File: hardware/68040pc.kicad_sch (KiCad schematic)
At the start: 1 part

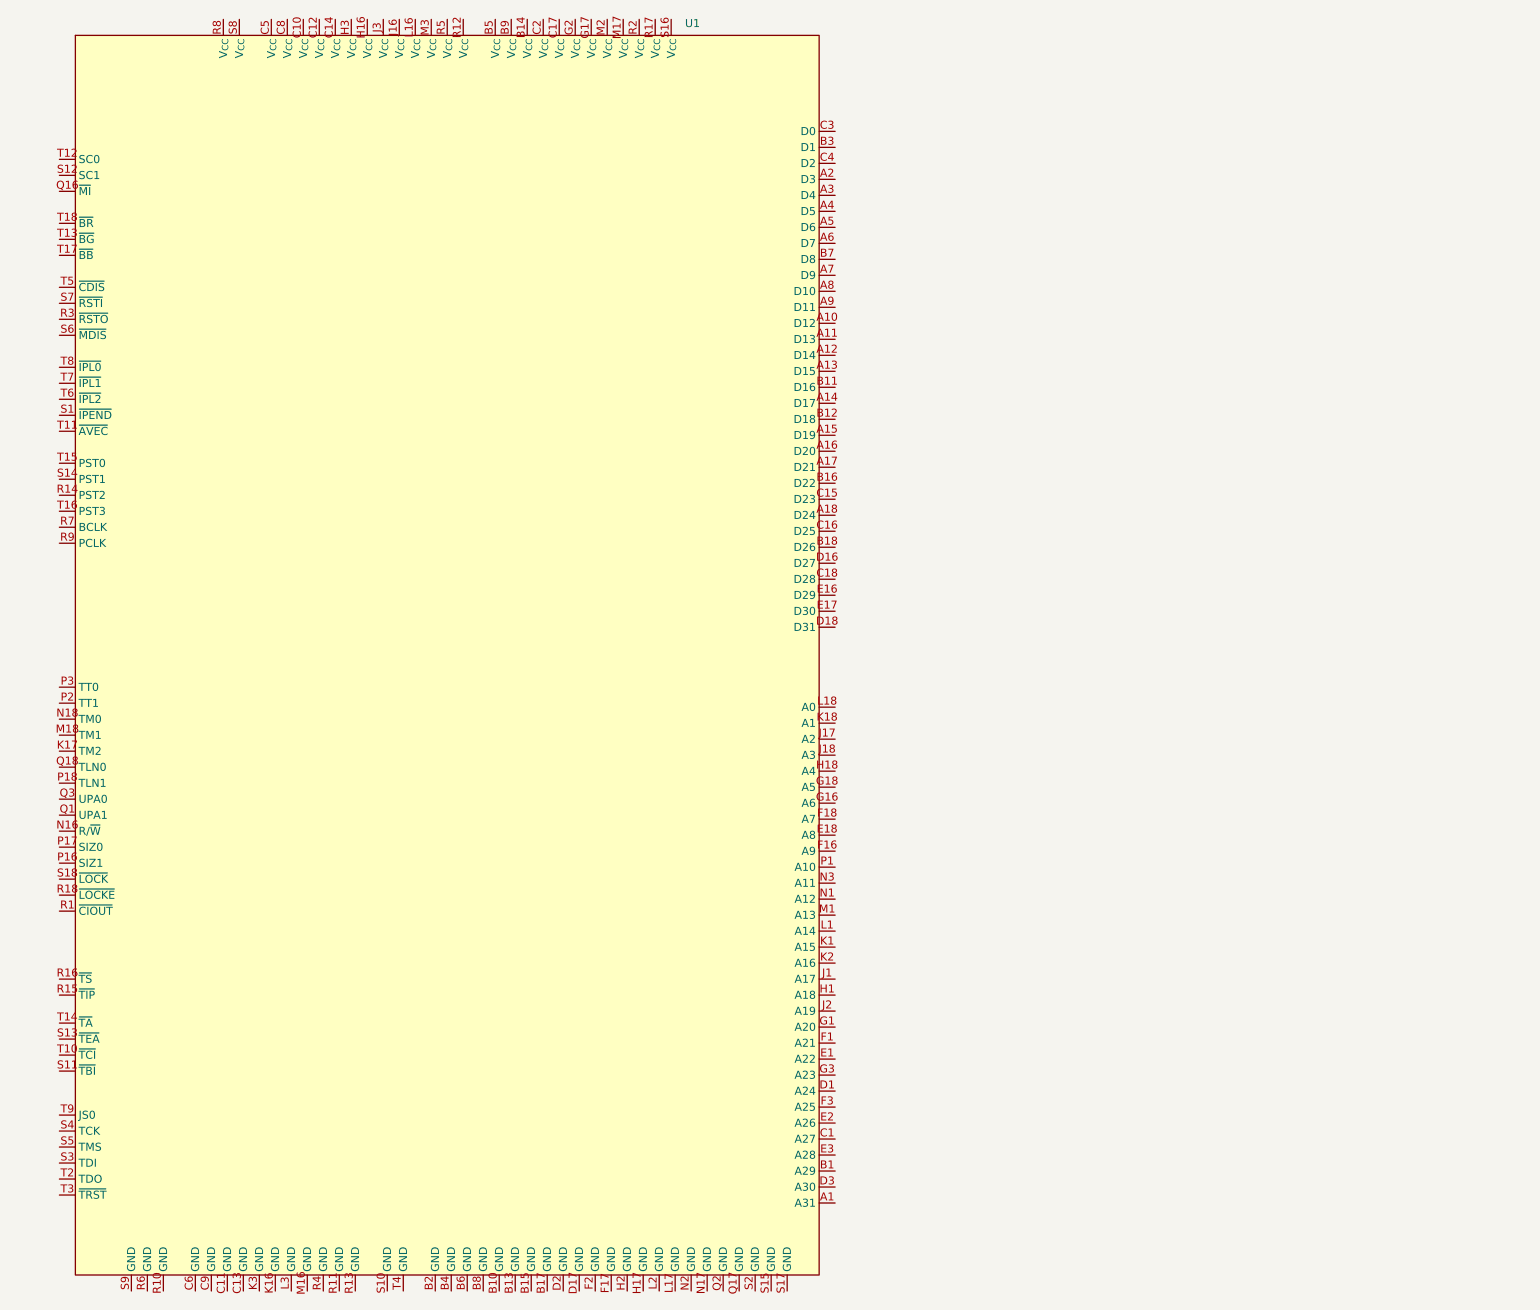
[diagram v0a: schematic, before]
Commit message: add atx outline, begin DRAM schematic
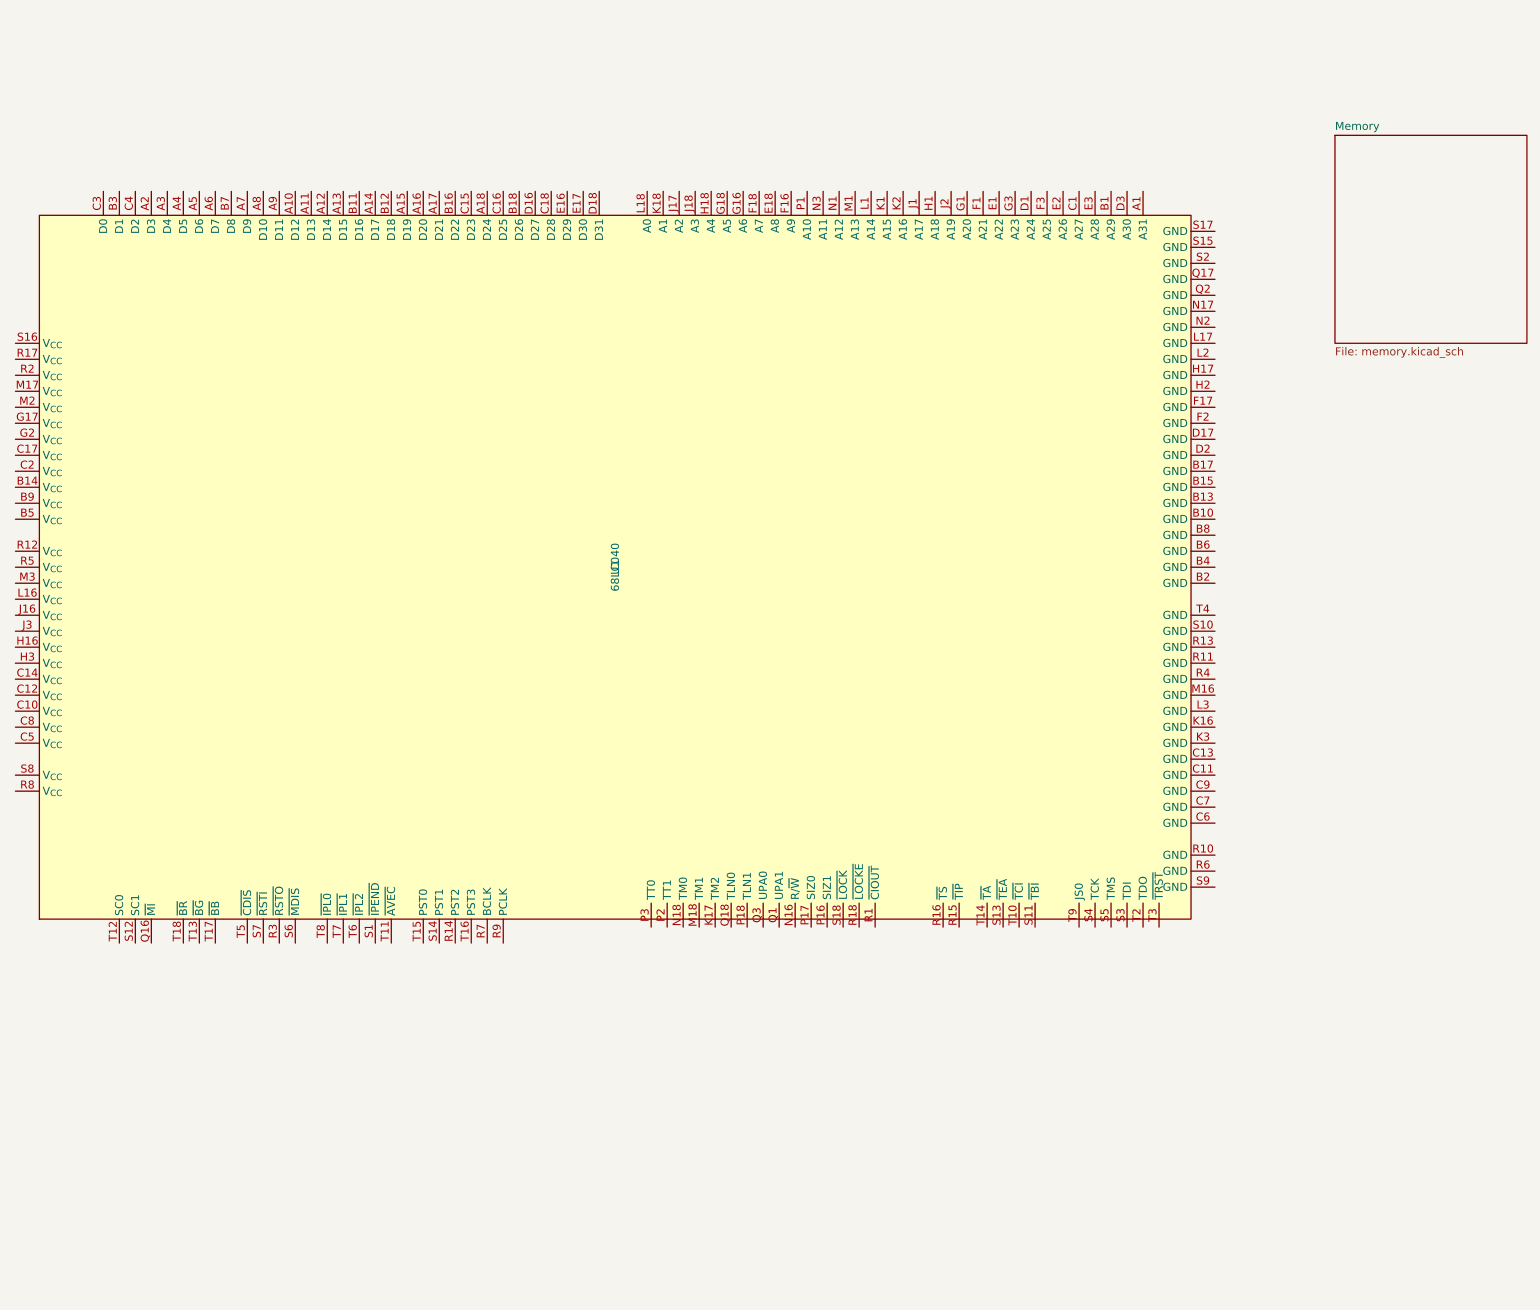
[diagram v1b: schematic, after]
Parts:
- removed U1: ~, 68040:PGA179, symbol 68040:68040
- added U1: 68LC040, 68040:PGA179, symbol 68040:68LC040
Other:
- added sheet Memory (memory.kicad_sch)
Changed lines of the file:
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@@
 (kicad_sch (version 20230121) (generator eeschema)
   (paper "A4")
-  (symbol (lib_id "68040:68040") (at 97.79 102.87 0) (unit 1)
+  (symbol (lib_id "68040:68LC040") (at 124.46 88.9 90) (unit 1)
     (in_bom yes) (on_board yes) (dnp no) (fields_autoplaced)
-    (property "Reference" "U1" (at 135.5441 2.54 0)
-      (effects (font (size 1.27 1.27)) (justify left))
-    )
-    (property "Value" "~" (at 97.79 102.87 0)
+    (property "Reference" "U1" (at 124.46 88.9 0)
       (effects (font (size 1.27 1.27)))
     )
-    (property "Footprint" "68040:PGA179" (at 97.79 102.87 0)
+    (property "Value" "68LC040" (at 124.46 88.9 0)
+      (effects (font (size 1.27 1.27)))
+    )
+    (property "Footprint" "68040:PGA179" (at 124.46 88.9 0)
       (effects (font (size 1.27 1.27)) hide)
     )
-    (property "Datasheet" "" (at 97.79 102.87 0)
+    (property "Datasheet" "" (at 124.46 88.9 0)
       (effects (font (size 1.27 1.27)) hide)
     )
@@
     (pin "C5")
     (pin "C6")
+    (pin "C7")
     (pin "C8")
     (pin "C9")
@@
       )
     )
+  )
+  (sheet (at 238.76 20.32) (size 30.48 33.02) (fields_autoplaced)
+    (stroke (width 0.1524) (type solid))
+    (fill (color 0 0 0 0.0000))
+    (property "Sheetname" "Memory" (at 238.76 19.6084 0)
+      (effects (font (size 1.27 1.27)) (justify left bottom))
+    )
+    (property "Sheetfile" "memory.kicad_sch" (at 238.76 53.9246 0)
+      (effects (font (size 1.27 1.27)) (justify left top))
+    )
+    (instances
+      (project "68040pc"
+        (path "/3006deba-2100-40f8-9f39-987a5c2c14c7" (page "2"))
+      )
+    )

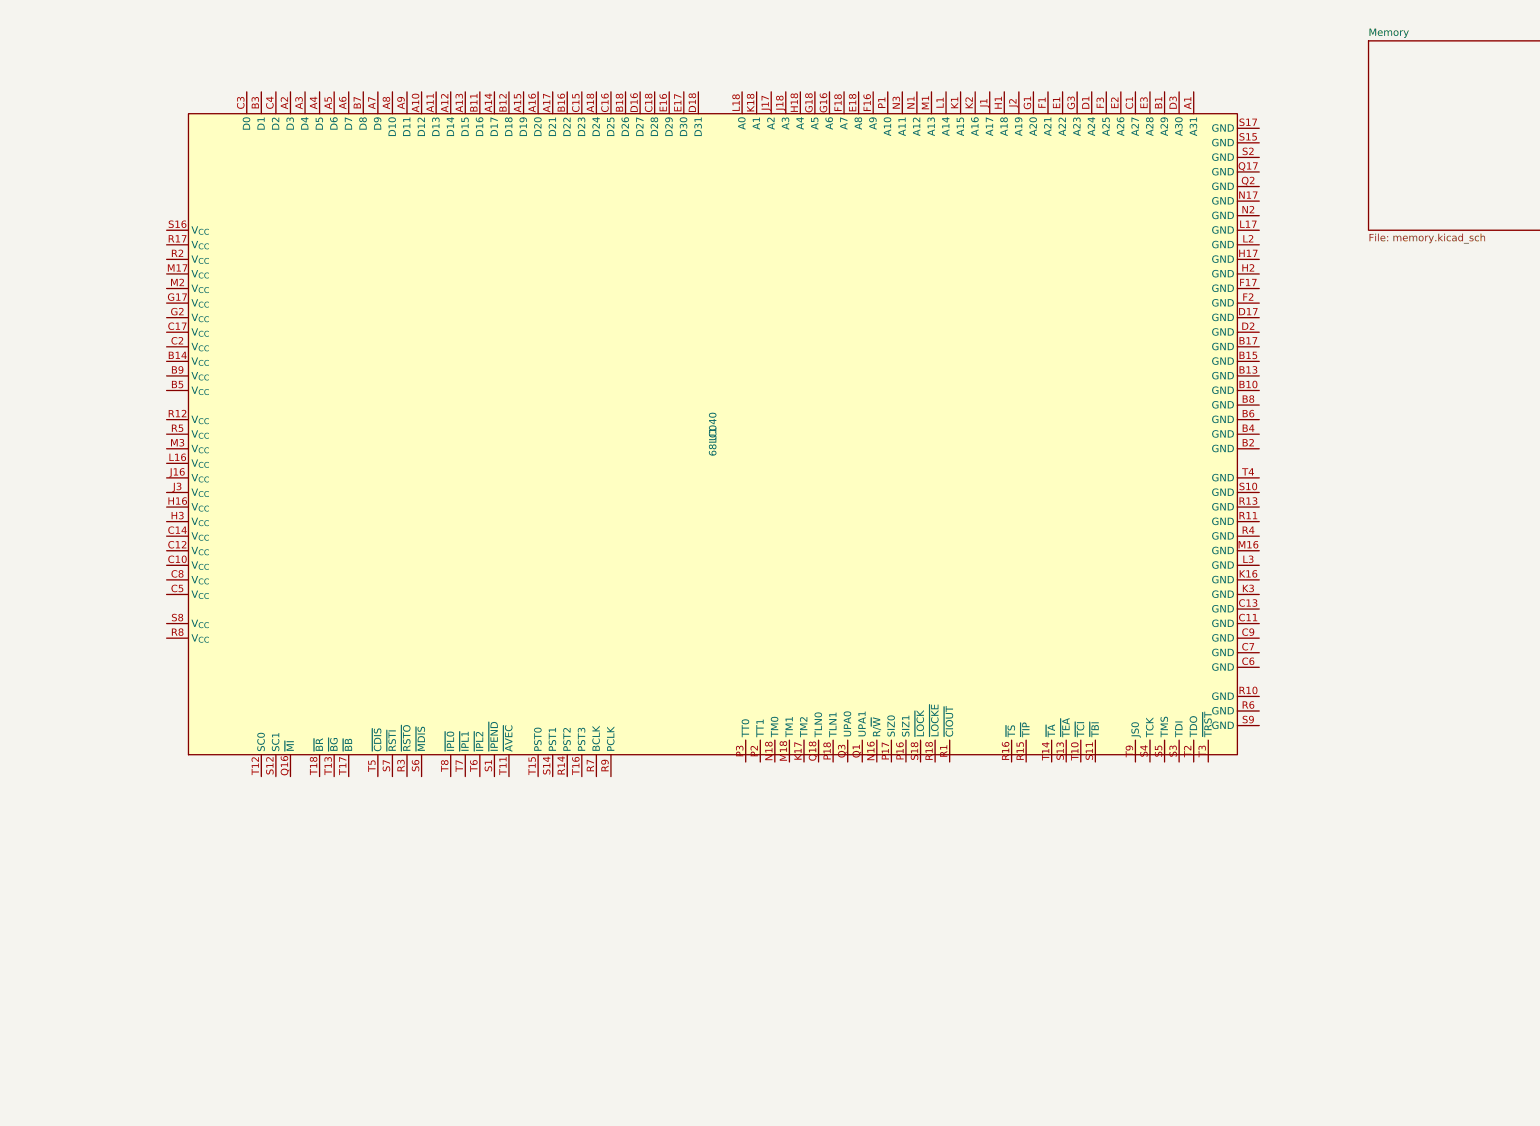
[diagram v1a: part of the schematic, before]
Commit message: more memory wiring
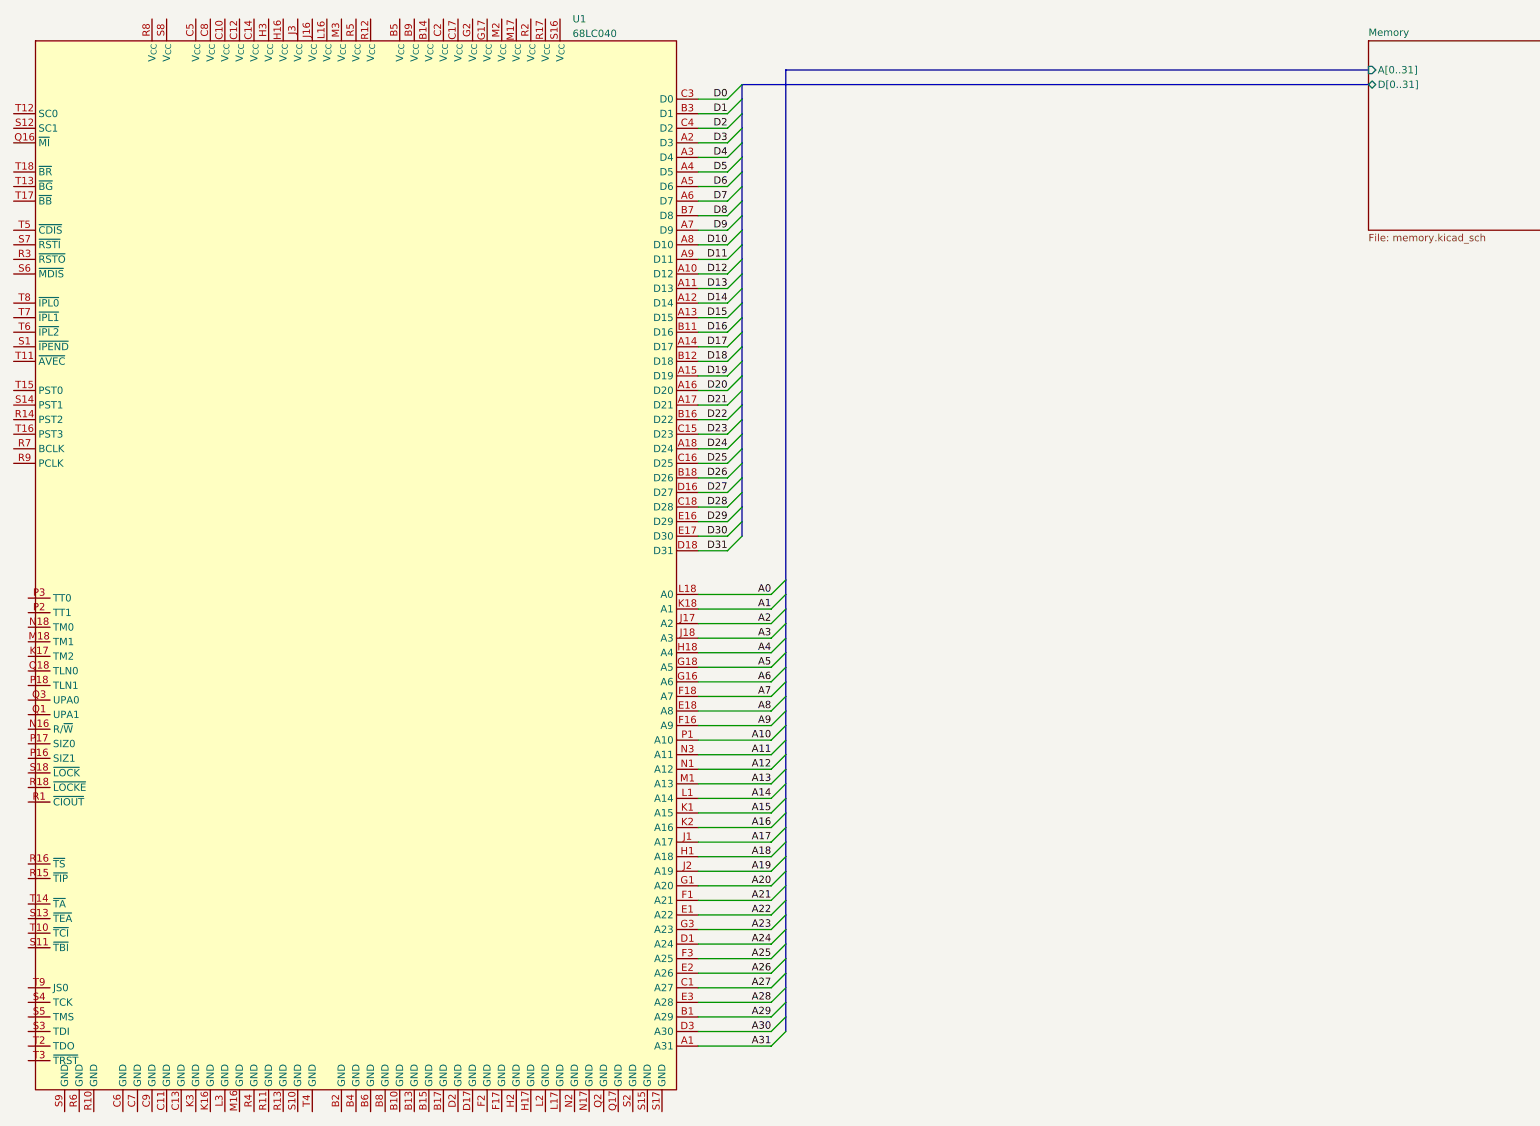
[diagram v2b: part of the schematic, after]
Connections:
- net A31: now reaches U1.A1 (A31)
- net D12: now reaches U1.A10 (D12)
- net D13: now reaches U1.A11 (D13)
- net D14: now reaches U1.A12 (D14)
- net D15: now reaches U1.A13 (D15)
- net D17: now reaches U1.A14 (D17)
- net D19: now reaches U1.A15 (D19)
- net D20: now reaches U1.A16 (D20)
- net D21: now reaches U1.A17 (D21)
- net D24: now reaches U1.A18 (D24)
- net D3: now reaches U1.A2 (D3)
- net D4: now reaches U1.A3 (D4)
- net D5: now reaches U1.A4 (D5)
- net D6: now reaches U1.A5 (D6)
- net D7: now reaches U1.A6 (D7)
- net D9: now reaches U1.A7 (D9)
- net D10: now reaches U1.A8 (D10)
- net D11: now reaches U1.A9 (D11)
- net A29: now reaches U1.B1 (A29)
- net D16: now reaches U1.B11 (D16)
- net D18: now reaches U1.B12 (D18)
- net D22: now reaches U1.B16 (D22)
- net D26: now reaches U1.B18 (D26)
- net D1: now reaches U1.B3 (D1)
- net D8: now reaches U1.B7 (D8)
- net A27: now reaches U1.C1 (A27)
- net D23: now reaches U1.C15 (D23)
- net D25: now reaches U1.C16 (D25)
- net D28: now reaches U1.C18 (D28)
- net D0: now reaches U1.C3 (D0)
- net D2: now reaches U1.C4 (D2)
- net A24: now reaches U1.D1 (A24)
- net D27: now reaches U1.D16 (D27)
- net D31: now reaches U1.D18 (D31)
- net A30: now reaches U1.D3 (A30)
- net A22: now reaches U1.E1 (A22)
- net D29: now reaches U1.E16 (D29)
- net D30: now reaches U1.E17 (D30)
- net A8: now reaches U1.E18 (A8)
- net A26: now reaches U1.E2 (A26)
- net A28: now reaches U1.E3 (A28)
- net A21: now reaches U1.F1 (A21)
- net A9: now reaches U1.F16 (A9)
- net A7: now reaches U1.F18 (A7)
- net A25: now reaches U1.F3 (A25)
- net A20: now reaches U1.G1 (A20)
- net A6: now reaches U1.G16 (A6)
- net A5: now reaches U1.G18 (A5)
- net A23: now reaches U1.G3 (A23)
- net A18: now reaches U1.H1 (A18)
- net A4: now reaches U1.H18 (A4)
- net A17: now reaches U1.J1 (A17)
- net A2: now reaches U1.J17 (A2)
- net A3: now reaches U1.J18 (A3)
- net A19: now reaches U1.J2 (A19)
- net A15: now reaches U1.K1 (A15)
- net A1: now reaches U1.K18 (A1)
- net A16: now reaches U1.K2 (A16)
- net A14: now reaches U1.L1 (A14)
- net A0: now reaches U1.L18 (A0)
- net A13: now reaches U1.M1 (A13)
- net A12: now reaches U1.N1 (A12)
- net A11: now reaches U1.N3 (A11)
- net A10: now reaches U1.P1 (A10)
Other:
- sheet Memory ports: added A[0..31], D[0..31]; removed none
- moved on the sheet: U1
